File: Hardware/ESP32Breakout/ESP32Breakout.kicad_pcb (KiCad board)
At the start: 2 copper layers, 80 x 59.7 mm, 36 parts, among them J1 8P8C, J10 ESP32 BO L, J11 RJ45 BO, J12 CAN BO, J2 LCD Header, J3 USB_B_Micro, J4 Conn_01x02_Male, J5 Screw_Terminal_01x05, J6 USBConn BO, J7 USB BO L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

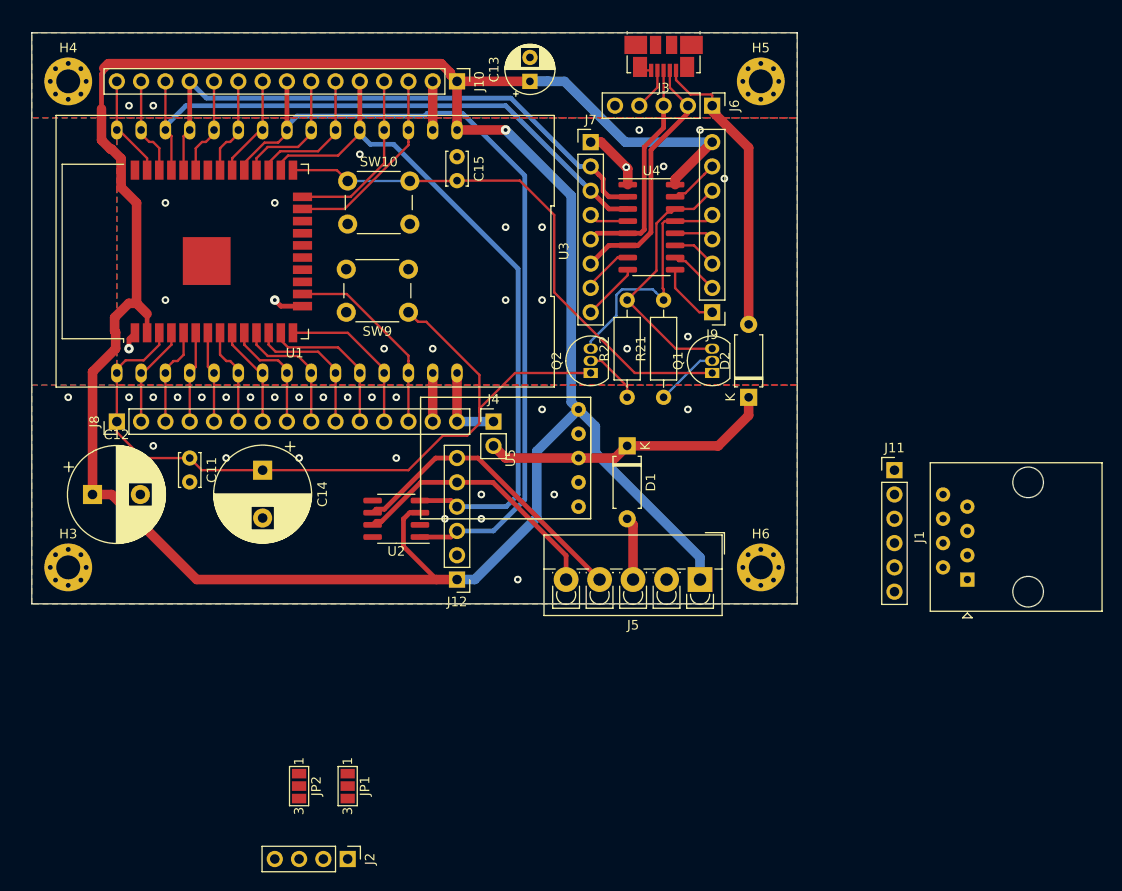
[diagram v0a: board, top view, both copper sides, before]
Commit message: Fixup of holes and labels
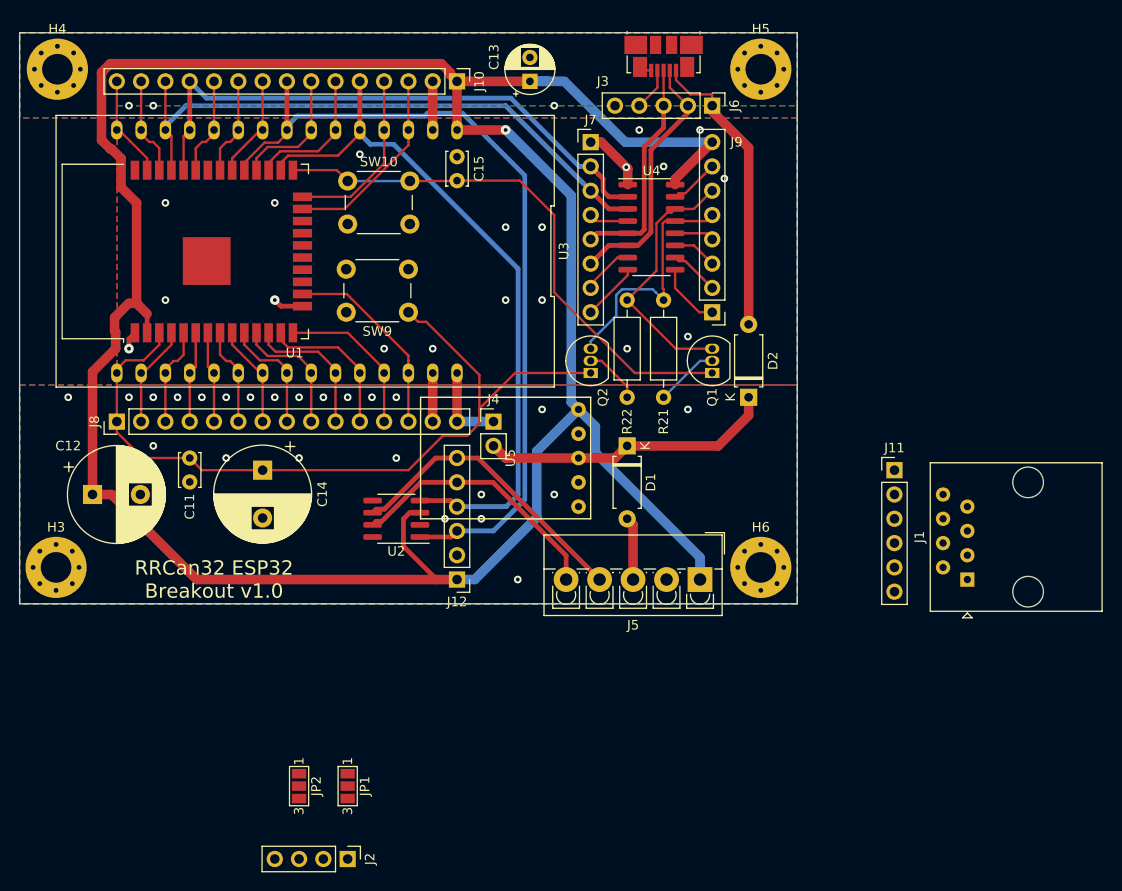
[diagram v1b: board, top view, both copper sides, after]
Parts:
- H3, H4, H5, H6: footprint MountingHole:MountingHole_2.5mm_Pad_Via -> MountingHole:MountingHole_3.2mm_M3_Pad_Via
- moved H4 1.70 mm to (21.7, 21.6)
- moved H3 1.27 mm to (21.6, 73.7)
- moved H5 1.27 mm to (95.2, 21.6)
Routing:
- net GND: vias 45 -> 46
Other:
- board size 80 x 59.7 mm -> 81.3 x 59.7 mm
- board text added: "RRCan32 ESP32 Breakout v1.0"

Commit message: Updated all boards
ESP32Breakout now with S88 driver.
ESP32Breakout has the auto-reset circut removed.
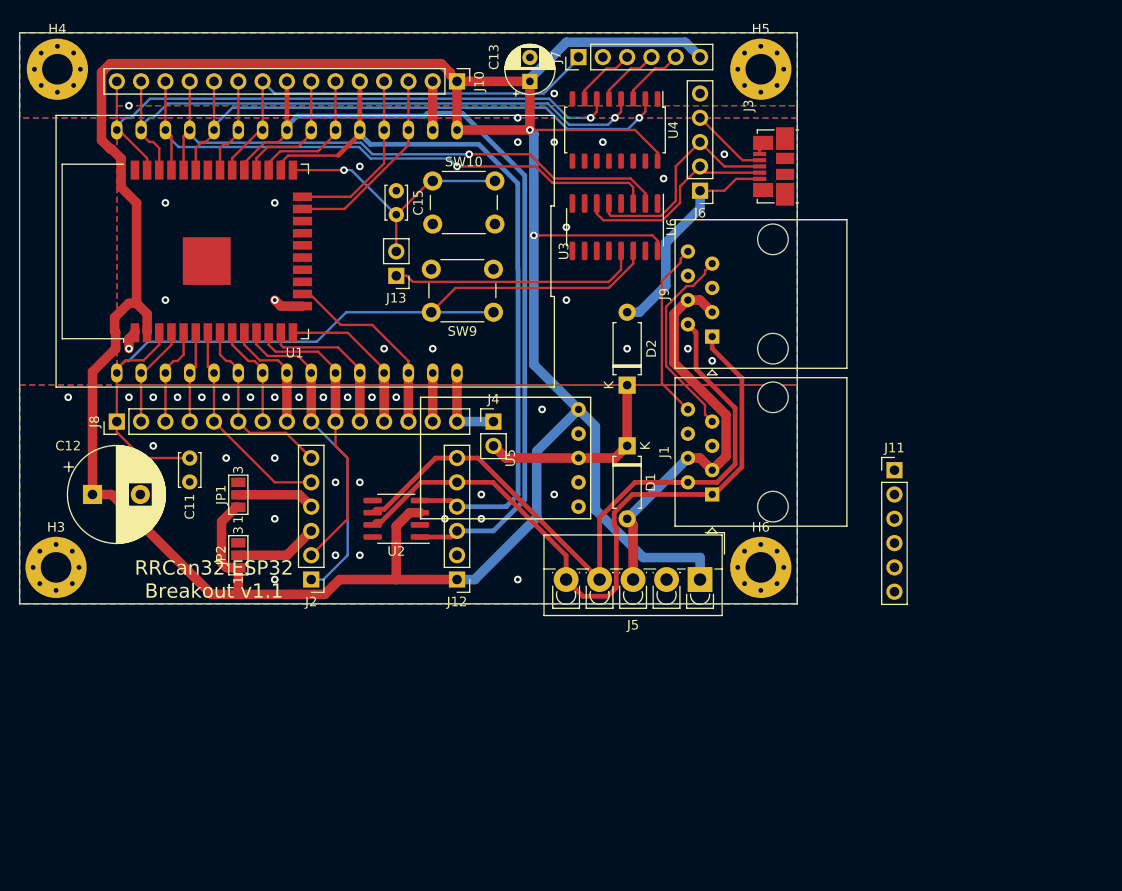
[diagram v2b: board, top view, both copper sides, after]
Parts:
- removed C14: 10u, Capacitor_THT:CP_Radial_D10.0mm_P5.00mm
- removed Q1, Q2: BC547, Package_TO_SOT_THT:TO-92_Inline
- removed R21, R22: 10k, Resistor_THT:R_Axial_DIN0207_L6.3mm_D2.5mm_P10.16mm_Horizontal
- added J13: Conn_01x02_Male, Connector_PinHeader_2.54mm:PinHeader_1x02_P2.54mm_Vertical, F.Cu at (57.1, 43.2)
- added U6: CH340G, Package_SO:SOIC-16_3.9x9.9mm_P1.27mm, F.Cu at (80.0, 38.1)
- J2: footprint Connector_PinHeader_2.54mm:PinHeader_1x04_P2.54mm_Vertical -> Connector_PinHeader_2.54mm:PinHeader_1x06_P2.54mm_Vertical
- J7: value USB BO L -> S88 Header; footprint Connector_PinHeader_2.54mm:PinHeader_1x08_P2.54mm_Vertical -> Connector_PinHeader_2.54mm:PinHeader_1x06_P2.54mm_Vertical
- J9: value USB BO R -> 8P8C; footprint Connector_PinHeader_2.54mm:PinHeader_1x08_P2.54mm_Vertical -> Connector_RJ:RJ45_Amphenol_54602-x08_Horizontal
- U2: value TJA1051T -> SN65HVD230
- U4: value CH340C -> 74LS367; footprint Package_SO:SOIC-16_3.9x9.9mm_P1.27mm -> Package_SO:SOP-16_4.55x10.3mm_P1.27mm
- moved JP1 32.5 mm to (40.6, 66.1), turned to 90 degrees
- moved J2 29.5 mm to (48.3, 74.9), turned to 180 degrees
- moved J1 28.1 mm to (90.2, 66.0)
- moved JP2 25.0 mm to (40.6, 72.4), turned to 90 degrees
- moved J3 16.3 mm to (96.6, 31.8), turned to 90 degrees
- moved D2 12.8 mm to (81.3, 54.6)
- moved U4 10.9 mm to (80.0, 27.9), turned to 270 degrees
- moved J6 8.98 mm to (88.9, 34.3), turned to 180 degrees
- moved J7 8.98 mm to (76.2, 20.3), turned to 90 degrees
- moved SW10 8.89 mm to (61.0, 33.3)
- moved SW9 8.89 mm to (67.3, 47.0)
- moved C15 7.28 mm to (57.1, 34.3)
- moved J9 2.54 mm to (90.2, 49.5), turned to 90 degrees
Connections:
- net /F0 renamed /IO12
- net /F1 renamed /IO13
- net /F2 renamed /IO15
- net /F3 renamed /IO14
- net /F4 renamed /IO17
- net /Shift renamed /IO16
- J10 pad 10: /Encoder_A -> /IO19
- J10 pad 11: /EncoderB -> /S88_RESET_UC
- J10 pad 14: /Encoder_Button -> /S88_PS_UC
- J10 pad 15: /IO23 -> /S88_CLOCK_UC
- J10 pad 9: /Stop -> /S88_DATA
- J2 pad 1: Net-(J2-Pad1) -> /I2C_SCL
- J2 pad 2: Net-(J2-Pad2) -> /I2C_SDA
- J2 pad 3: /I2C_SDA -> Net-(J2-Pad3)
- J2 pad 4: /I2C_SCL -> Net-(J2-Pad4)
- J7 pad 1: GND -> /S88_DATA
- J7 pad 2: /BOARD_RX0 -> GND
- J7 pad 3: /BOARD_TX0 -> /S88_CLOCK
- J7 pad 4: Net-(J7-Pad4) -> /S88_PS
- J7 pad 5: /USB+ -> /S88_RESET
- J7 pad 6: /USB- -> VCC
- J8 pad 4: /S88_DATA -> /IO34
- J8 pad 5: /S88_CLOCK_UC -> /Encoder_A
- J8 pad 6: /S88_PS_UC -> /EncoderB
- J8 pad 7: /S88_RESET_UC -> /IO33
- J9 pad 1: Net-(J9-Pad1) -> /CANH
- J9 pad 2: Net-(J9-Pad2) -> /CANL
- J9 pad 3: Net-(J9-Pad3) -> /VinCAN
- J9 pad 4: Net-(J9-Pad4) -> /VinCAN
- J9 pad 5: /!DTR -> GND
- J9 pad 6: /!RTS -> GND
- J9 pad 7: Net-(J9-Pad7) -> Net-(J1-Pad7)
- J9 pad 8: VCC -> Net-(J1-Pad8)
- JP1 pad 2: Net-(J2-Pad1) -> Net-(J2-Pad4)
- JP2 pad 2: Net-(J2-Pad2) -> Net-(J2-Pad3)
- U1 pad 30: /Stop -> /S88_DATA
- U1 pad 31: /Encoder_A -> /IO19
- U1 pad 33: /EncoderB -> /S88_RESET_UC
- U1 pad 36: /Encoder_Button -> /S88_PS_UC
- U1 pad 37: /IO23 -> /S88_CLOCK_UC
- U1 pad 6: /S88_DATA -> /IO34
- U1 pad 7: /S88_CLOCK_UC -> /Encoder_A
- U1 pad 8: /S88_PS_UC -> /EncoderB
- U1 pad 9: /S88_RESET_UC -> /IO33
- U2 pad 8: (no net) -> GND
- U3 pad 10: /Encoder_A -> /IO19
- U3 pad 11: /EncoderB -> /S88_RESET_UC
- U3 pad 14: /Encoder_Button -> /S88_PS_UC
- U3 pad 15: /IO23 -> /S88_CLOCK_UC
- U3 pad 19: /S88_DATA -> /IO34
- U3 pad 20: /S88_CLOCK_UC -> /Encoder_A
- U3 pad 21: /S88_PS_UC -> /EncoderB
- U3 pad 22: /S88_RESET_UC -> /IO33
- U3 pad 9: /Stop -> /S88_DATA
- U4 pad 10: Net-(J9-Pad2) -> GND
- U4 pad 11: Net-(J9-Pad3) -> (no net)
- U4 pad 12: Net-(J9-Pad4) -> GND
- U4 pad 13: /!DTR -> (no net)
- U4 pad 14: /!RTS -> GND
- U4 pad 15: Net-(J9-Pad7) -> GND
- U4 pad 2: /BOARD_RX0 -> /S88_RESET_UC
- U4 pad 3: /BOARD_TX0 -> /S88_RESET
- U4 pad 4: Net-(J7-Pad4) -> /S88_PS_UC
- U4 pad 5: /USB+ -> /S88_PS
- U4 pad 6: /USB- -> /S88_CLOCK_UC
- U4 pad 7: Net-(J7-Pad7) -> /S88_CLOCK
- U4 pad 8: Net-(J7-Pad8) -> GND
- U4 pad 9: Net-(J9-Pad1) -> (no net)
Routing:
- net /S88_CLOCK_UC: track 9.55 -> 64.9 mm, vias 0 -> 1
- net /S88_PS_UC: track 10.5 -> 64.7 mm, vias 0 -> 1
- net /S88_RESET_UC: track 10.7 -> 59.6 mm, vias 0 -> 1
- net /CANH: track 27.7 -> 72.3 mm
- net VCC: track 268.7 -> 310.4 mm, vias 1 -> 2
- net /CANL: track 31.4 -> 71.0 mm
- net /S88_DATA: track 9.54 -> 46.0 mm
- net /VinCAN: track 6.61 -> 43.0 mm
- net /GPIO0: track 57.4 -> 28.4 mm, vias 0 -> 1
- net /!RTS: track 27.5 -> 0.00 mm
- net /GPIO0-SER: track 0.00 -> 26.3 mm
- net /!DTR: track 26.0 -> 0.00 mm
- net Net-(J1-Pad7): track 0.00 -> 20.9 mm
- net /I2C_SCL: track 13.5 -> 33.9 mm
- net Net-(J1-Pad8): track 0.00 -> 18.8 mm
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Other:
- board text added: "RRCan32 ESP32 Breakout v1.1"
- board text removed: "RRCan32 ESP32 Breakout v1.0"

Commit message: Fixes on the breakout board
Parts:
- moved J11 32.1 mm to (83.0, 45.0)
- moved D2 3.28 mm to (78.0, 54.6)
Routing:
- net /CANH: track 72.3 -> 85.4 mm
- net /CANL: track 71.0 -> 82.5 mm
- net /VinCAN: track 43.0 -> 53.6 mm, vias 0 -> 1
- net Net-(J1-Pad7): track 20.9 -> 27.5 mm
- net /VinCommon: track 21.4 -> 23.4 mm
- net Net-(J1-Pad8): track 18.8 -> 20.5 mm
- net /VinUsb: track 23.3 -> 25.0 mm
- net GND: vias 49 -> 53
